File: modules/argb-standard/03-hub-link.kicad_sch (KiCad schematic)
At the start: 5 parts, among them J2 TO-HUB

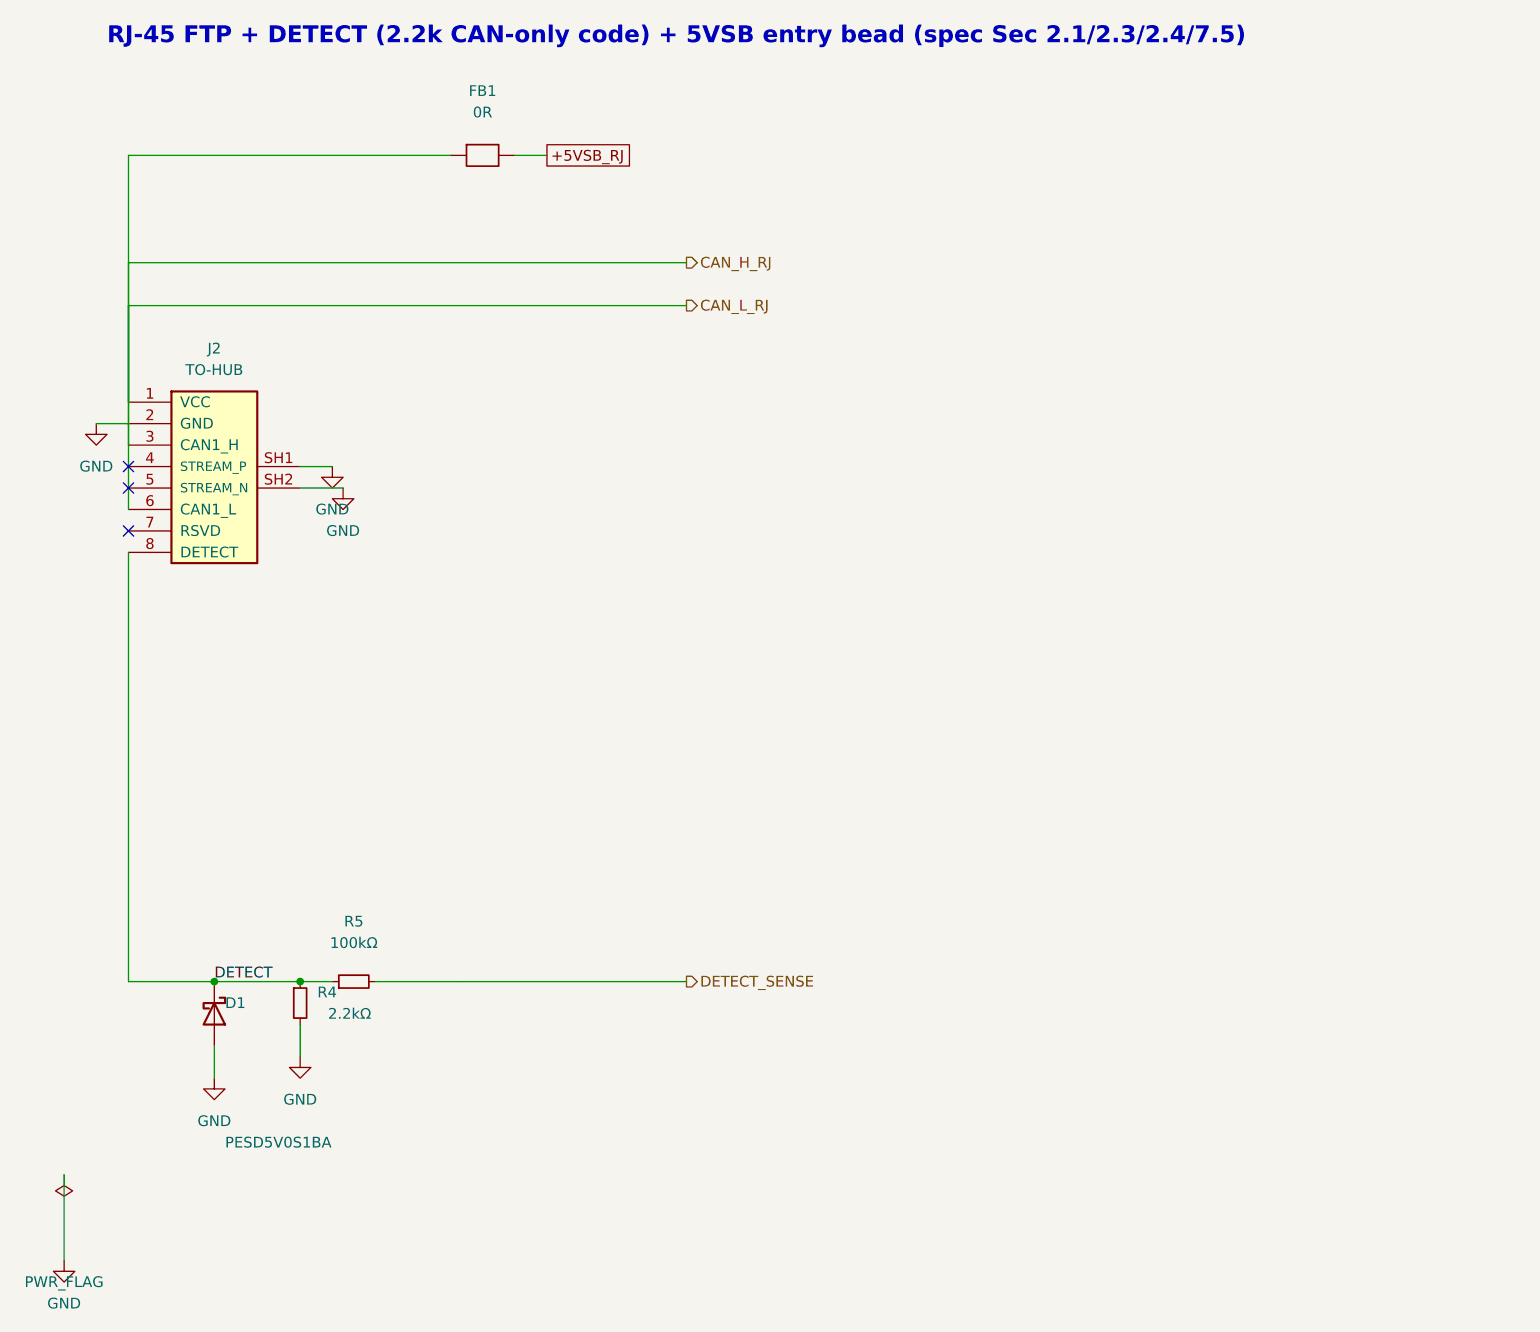
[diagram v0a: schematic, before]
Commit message: ARGB Controller Standard schematic LANDED: 8-leaf hierarchical design, coordinator-verified
- All gates re-verified independently: ERC 0 errors at severity-error; netlist 103 nets / 81 comps; USB-C nets (VBUS/CC1/CC2/D+/D-) proven isolated (the agent's netlist inspection caught + fixed a column-routing merge of all five — a class audit-sch cannot see); DETECT chain = 2.2k code + PESD + poke-tap exactly per SS2.3/SS2.4; CAN + sensed +5V_LED rail + 8x LED channel chains verified; audit-sch ok; containment/bounds clean x9; lib tables fully cec-namespaced (the vendor-verify FAIL is the pre-existing ent-common-local nickname, ENT lane)
- Design per spec SS7: SATA 5V-direct front end (AO4407A P-FET + 2920L polyfuse + MF72 NTC inrush), total shunt + INA180A2, 74AHCT244 + per-channel 330R/BAT54S/PESD into keyed 4-pin ARGB headers x8, TJA1051T/3 no-term, RJ-45 FTP + DETECT, USB-C data + SS6.14 standalone suite, SK6812 status pixel
- BOM ~8.30 USD raw (below the SS9 14-20 band; no fab/fees, SATA placeholder); agent's BOM cross-check fixed 6 real LCSC pointer errors
- FLAGGED FOR OWNER (README): OQ-29 MCU working basis = ESP32-S3-MINI-1 (8-ch parallel-out; C6 has only 2 RMT TX); RJ-45-VCC standby-OR proposal; BAT54W->BAT54S substitution; OQ-36 header keying; SATA connector consigned

Co-Authored-By: Claude Fable 5 <noreply@anthropic.com>
Claude-Session: https://claude.ai/code/session_01LvfqcnEeuin2oyJQw548EX
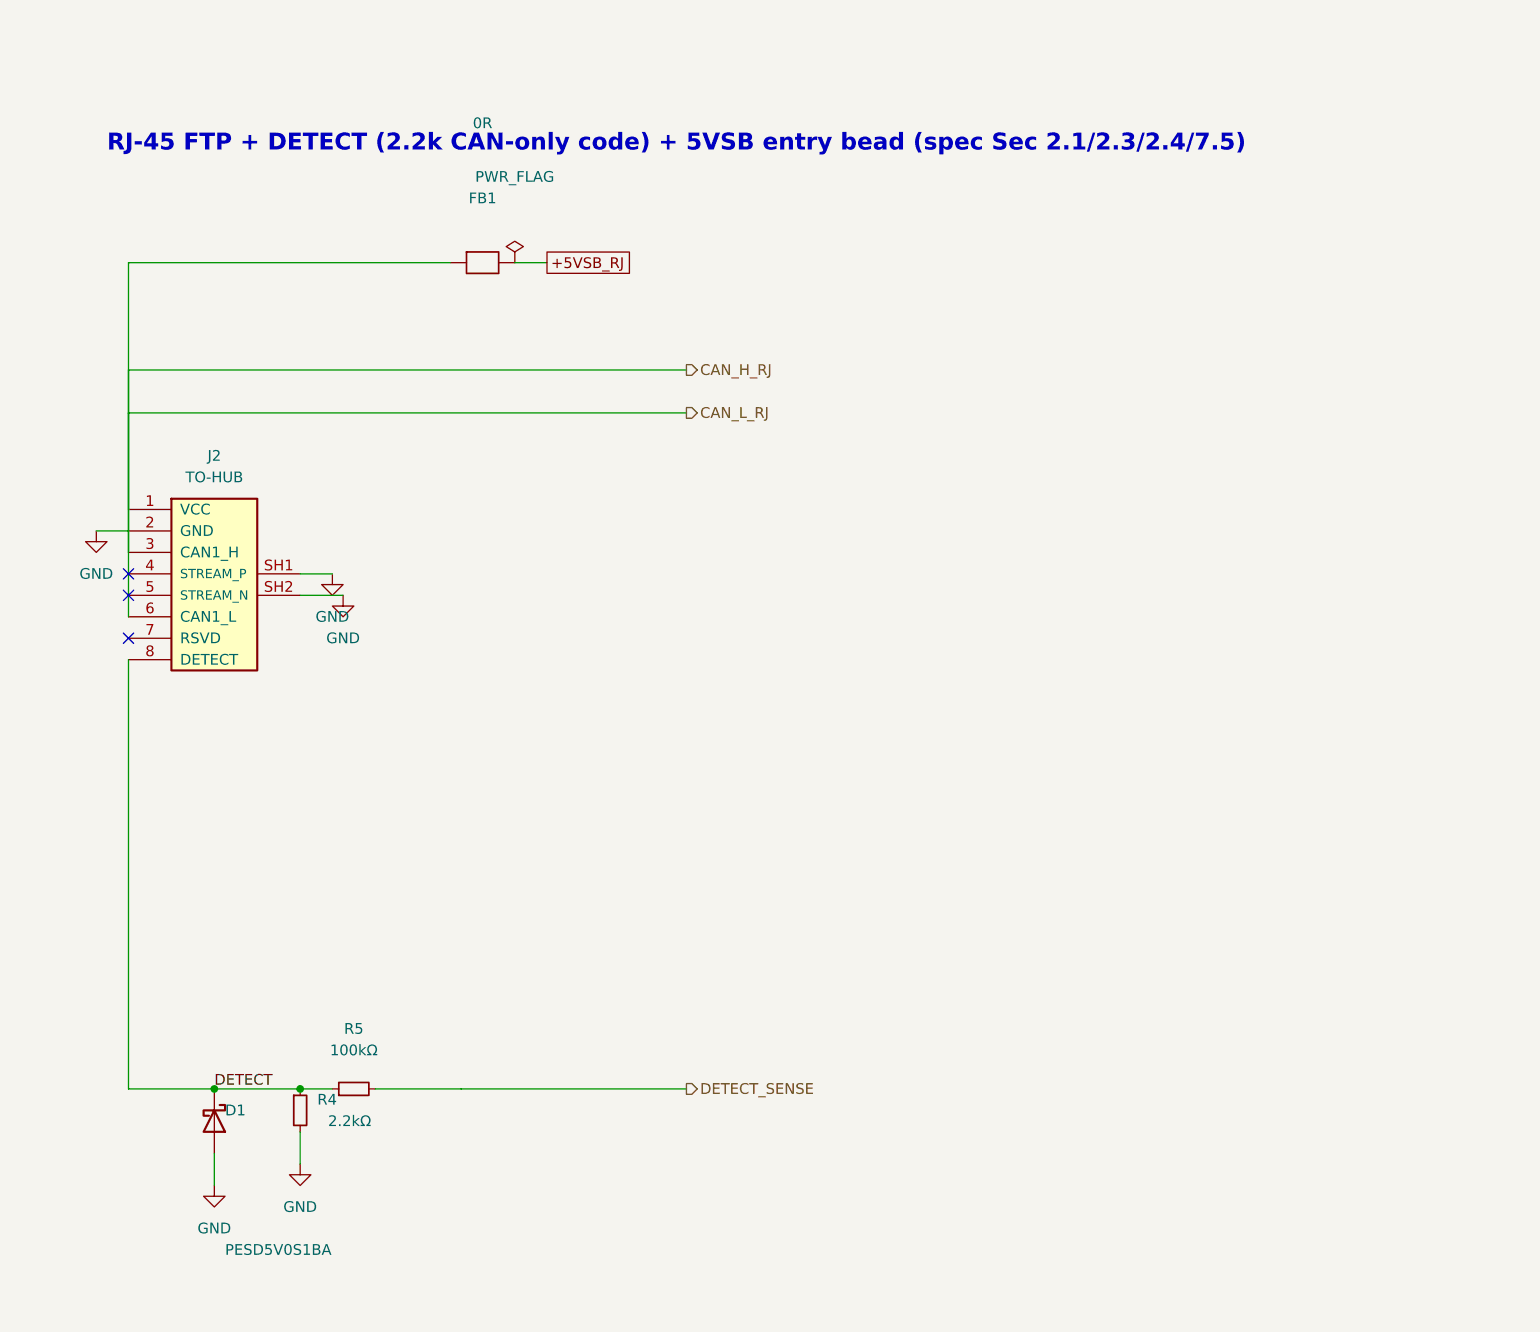
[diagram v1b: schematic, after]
